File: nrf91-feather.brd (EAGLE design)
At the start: 50.8 x 22.9 mm, 126 parts, among them J2 CON-HEADER-1X12-MALE-PIN, J3 CON-HEADER-1X16-MALE-PIN, J4 CON-1909763-1, J5 CON-SIM-104224-0820, J6 CON-S2B-PH-SM4-TB(LF)(SN), J7 CON-1909763-1, J8 CON-USB-DX07S016JA1R1500, J9 CON-TC2030-MCP-NL, Q1 MOSFET-N-SC89, Q2 MOSFET-DUAL-COMP-SOT563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

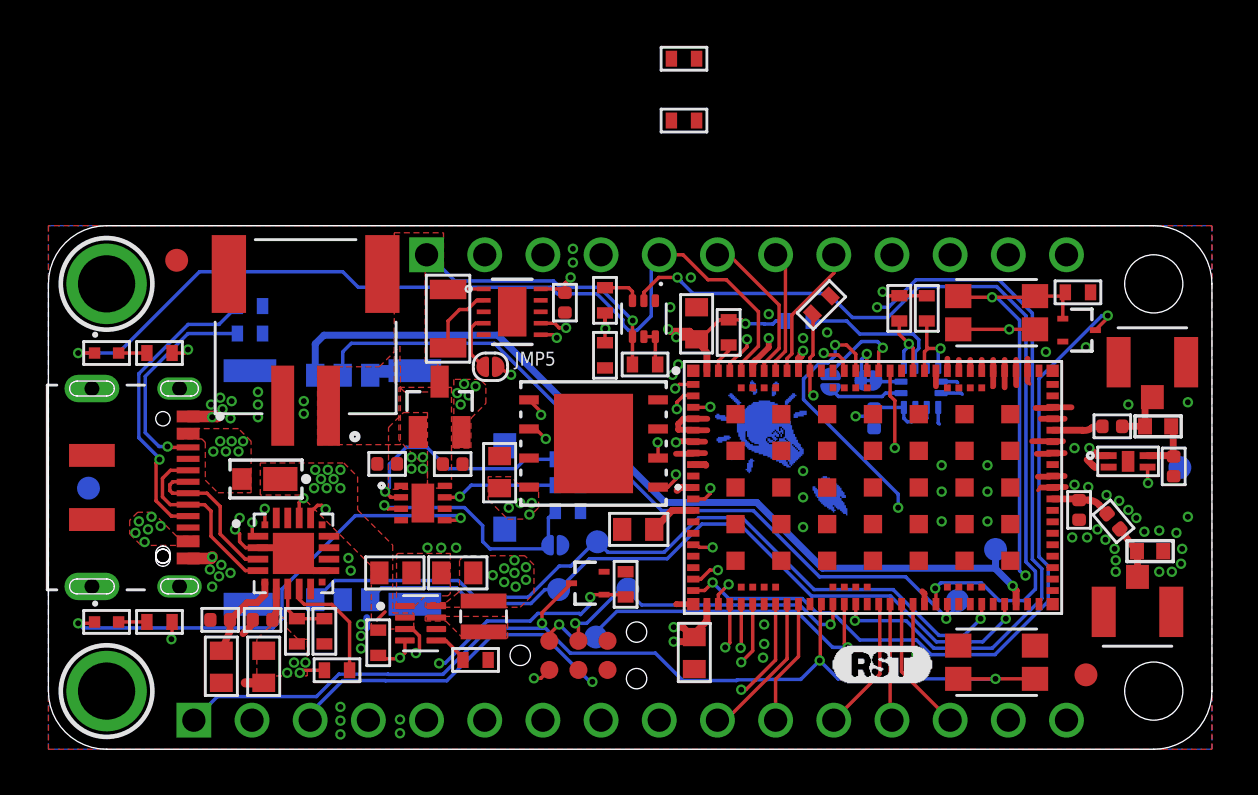
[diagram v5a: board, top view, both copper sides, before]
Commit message: Adding updated bypass and filtering for power supply
Changed:
* Ferrite and 47u for power inputs
* Re-routed battery measurement circuit
* Cleaned up
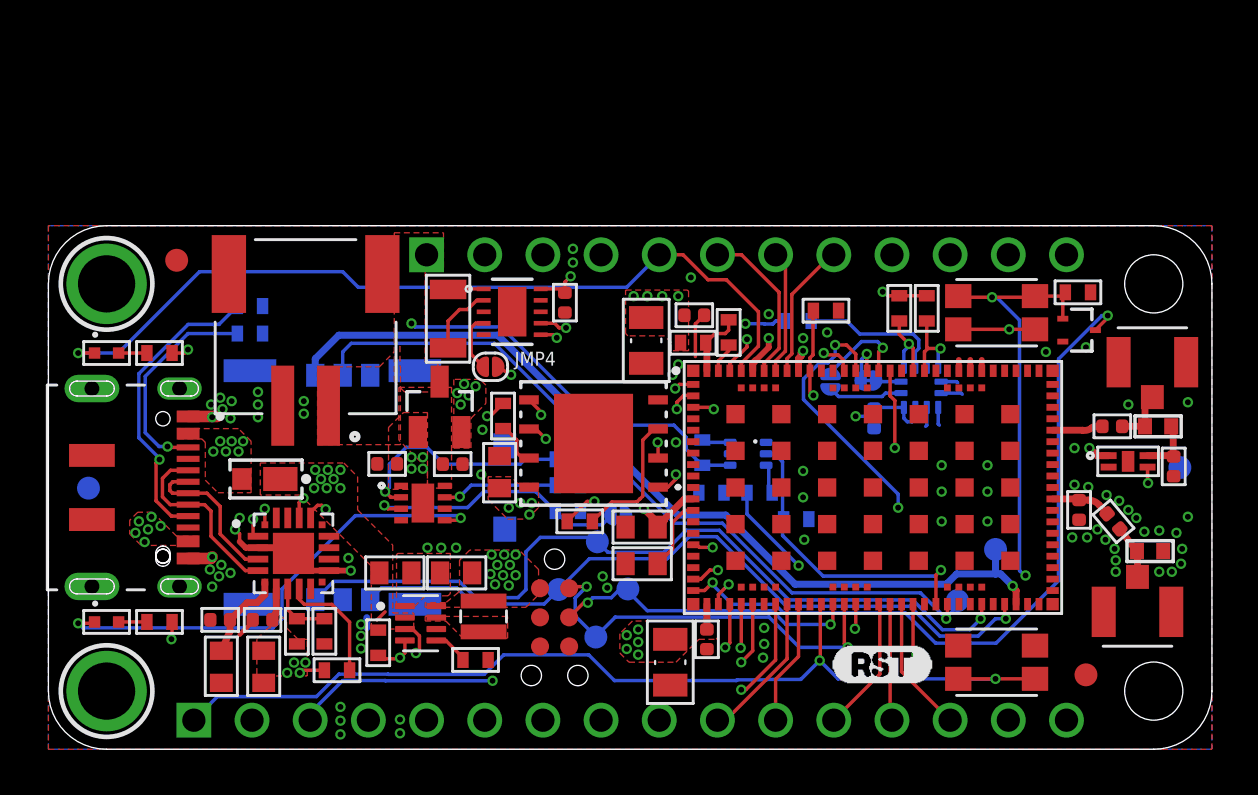
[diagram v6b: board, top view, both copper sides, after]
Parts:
- removed Q1: MOSFET-N-SC89, wolff-den:DIO_RB558WMF-L
- removed U$1: (no value), wolff-den:LOGO-CIRCUITDOJO-BULB
- added C20, C22: 0.1u, wolff-den:CAPC1005X55N
- added C21: 47u, wolff-den:C0805
- added FB1: FERRITE-120-100MHZ-0402, wolff-den:R0402-M
- C3: value 4.7u -> 47u; device wolff-den:C0603 -> wolff-den:C0805
- R9: value 100k -> 10k
- moved R23 18.1 mm to (23.2, 9.95), turned to 180 degrees
- moved R22 17.5 mm to (19.9, 14.6), turned to 90 degrees
- moved C3 14.8 mm to (27.1, 3.80), turned to 270 degrees
- moved R3 10.8 mm to (31.1, 11.2), flipped to the bottom, turned to 180 degrees
- moved R5 7.98 mm to (32.6, 10.1), flipped to the bottom, turned to 0 degrees
- moved R8 7.59 mm to (28.9, 11.2), flipped to the bottom, turned to 180 degrees
- moved Q2 7.45 mm to (30.6, 12.9), flipped to the bottom, turned to 0 degrees
- moved C8 5.96 mm to (25.9, 9.70), turned to 180 degrees
- moved R10 4.59 mm to (28.6, 12.9), flipped to the bottom, turned to 270 degrees
- moved J9 4.46 mm to (22.1, 8.30), turned to 270 degrees
- moved JMP2 3.04 mm to (24.9, 10.2)
- moved U$7 2.53 mm to (34.4, 6.30)
- moved C9 1.51 mm to (25.9, 8.10)
- moved U$6 0.78 mm to (30.3, 13.6)
- moved R1 0.32 mm to (34.0, 19.1), turned to 180 degrees
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- renumbered JMP5 to JMP4
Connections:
- removed net N$12: Q1.1, R5.2, U2.2
- new net N$16: FB1.2, R9.2, U1.102
- net !RESET: now also U2.2; no longer Q1.3
- net +3V3: now also C20.1, C21.1, C22.1, FB1.1; no longer R9.2, U1.102
- net GND: now also C20.2, C21.2, C22.2; no longer Q1.2
- net P0.25/VBAT_MEAS_EN: now also R5.2
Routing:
- net P0.20/VBAT_MEAS: track 47.3 -> 9.98 mm, vias 3 -> 2
- net P0.25/VBAT_MEAS_EN: track 37.0 -> 13.5 mm, vias 2 -> 1
- net N$12: track 22.1 -> 0.00 mm, vias 3 -> 0
- net GND: track 55.0 -> 33.1 mm, vias 84 -> 87
- net !RESET: track 46.8 -> 54.1 mm
- net N$9: track 0.00 -> 5.97 mm
- net VBAT: track 12.1 -> 16.8 mm
- net +3V3: track 21.6 -> 18.2 mm, vias 23 -> 31
- net P0.03/D7: track 39.7 -> 36.7 mm
- net N$16: track 0.00 -> 2.92 mm
- net FLASH_SCK: track 15.6 -> 12.7 mm
- net N$14: track 0.00 -> 1.99 mm
- net MODE/WAKE: track 54.9 -> 53.6 mm
- net N$5: track 2.06 -> 3.19 mm
- net CHG_TS: track 10.8 -> 11.8 mm
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
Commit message: Reconnect flash signals
Changed:
* Reconnect WP and HOLD signls
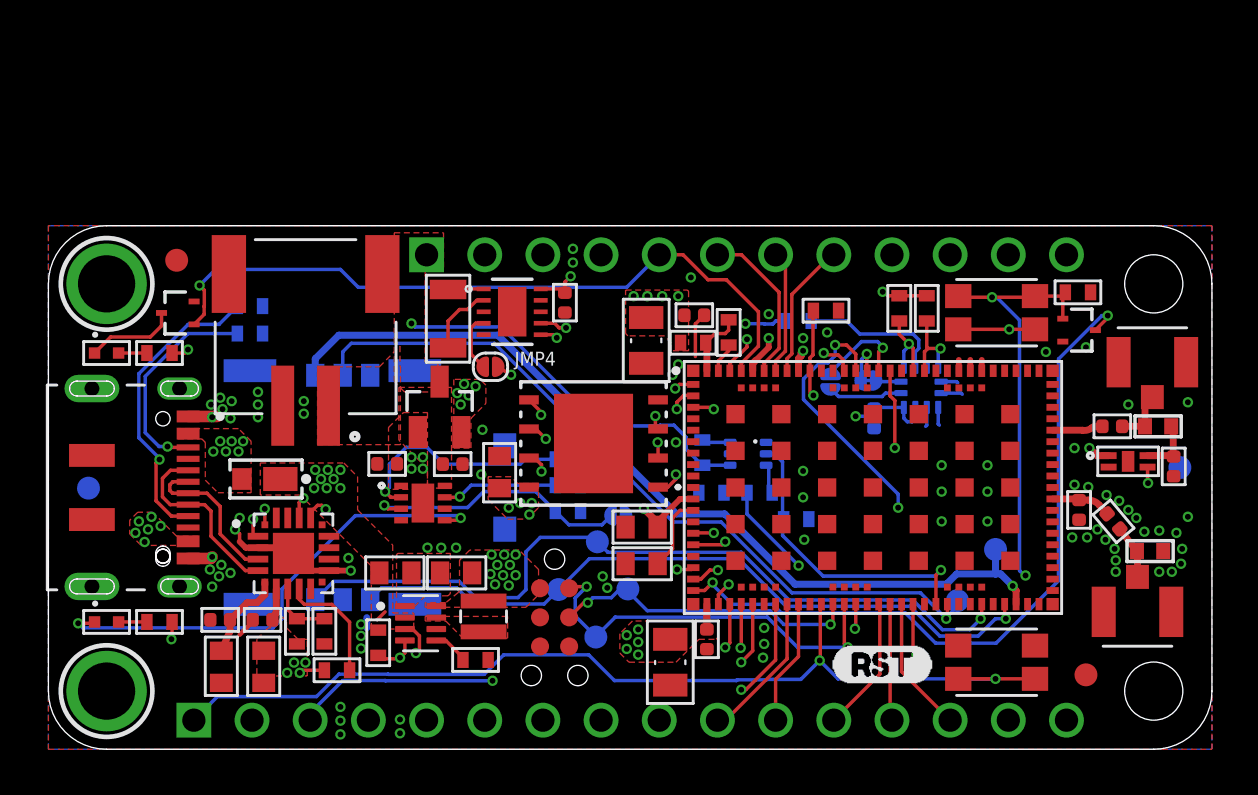
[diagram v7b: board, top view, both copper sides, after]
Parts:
- removed R22, R23: 100k, wolff-den:R0402-M
- added Q1: MOSFET-N-SC89, wolff-den:DIO_RB558WMF-L
- added R24: 100k, wolff-den:R0402-M
- R19: value 1M -> 100k
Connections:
- removed net N$14: R22.1, U6.7
- removed net N$9: R23.1, U6.3
- new net FLASH_HOLD: U1.18, U6.7
- new net FLASH_WP: U1.15, U6.3
- new net N$12: D3.C, Q1.3
- net +3V3: no longer R22.2, R23.2
- net GND: now also Q1.2, R24.1
- net P0.03/D7: now also Q1.1, R24.2; no longer D3.C
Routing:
- net FLASH_HOLD: track 0.00 -> 9.39 mm, vias 0 -> 2
- net FLASH_WP: track 0.00 -> 8.30 mm, vias 0 -> 2
- net N$9: track 5.97 -> 0.00 mm
- net P0.03/D7: track 36.7 -> 31.5 mm
- net +3V3: track 18.2 -> 13.8 mm, vias 31 -> 29
- net N$12: track 0.00 -> 3.98 mm
- net N$14: track 1.99 -> 0.00 mm
- net FLASH_SI: track 11.8 -> 12.7 mm
- net SIM_IO: track 32.3 -> 31.5 mm
- net SIM_CLK: track 35.1 -> 34.3 mm

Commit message: Consolidating parts
Changed:
* R9 to 1k
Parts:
- R9: value 10k -> 1k
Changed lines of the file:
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@@
 <attribute name="VALUE" x="5.54981875" y="6.5295" size="1.27013125" layer="28" rot="MR90"/>
 </element>
-<element name="R9" library="wolff-den" library_urn="urn:adsk.eagle:library:6370453" package="R0402-M" package3d_urn="urn:adsk.eagle:package:19061974/5" value="10k" x="29.7" y="18.2" smashed="yes" rot="R90">
-<attribute name="DESC" value="" x="17.6" y="-15.7" size="0.8128" layer="27" rot="R90" display="off"/>
-<attribute name="DIGIKEYPN" value="311-10.0KHRCT-ND" x="17.6" y="-15.7" size="0.8128" layer="27" rot="R90" display="off"/>
+<element name="R9" library="wolff-den" library_urn="urn:adsk.eagle:library:6370453" package="R0402-M" package3d_urn="urn:adsk.eagle:package:19061974/5" value="1k" x="29.7" y="18.2" smashed="yes" rot="R90">
+<attribute name="DESC" value="RES SMD 1K OHM 5% 1/16W 0402" x="17.6" y="-15.7" size="0.8128" layer="27" rot="R90" display="off"/>
+<attribute name="DIGIKEYPN" value="311-1.0KJRCT-ND" x="17.6" y="-15.7" size="0.8128" layer="27" rot="R90" display="off"/>
 <attribute name="MF" value="" x="17.6" y="-15.7" size="0.8128" layer="27" rot="R90" display="off"/>
-<attribute name="MPN" value="RC0603FR-0710KL" x="17.6" y="-15.7" size="0.8128" layer="27" rot="R90" display="off"/>
+<attribute name="MPN" value="RC0402JR-071KL" x="17.6" y="-15.7" size="0.8128" layer="27" rot="R90" display="off"/>
 <attribute name="NAME" x="29.7" y="18.2" size="0.2" layer="51" rot="R90" align="center"/>
-<attribute name="POWER" value="" x="17.6" y="-15.7" size="0.8128" layer="27" rot="R90" display="off"/>
-<attribute name="TEMPHIGH" value="155" x="29.7" y="18.2" size="1.778" layer="27" rot="R90" display="off"/>
-<attribute name="TEMPLOW" value="-55" x="29.7" y="18.2" size="1.778" layer="27" rot="R90" display="off"/>
-<attribute name="TOLERANCE" value="1%" x="17.6" y="-15.7" size="0.8128" layer="27" rot="R90" display="off"/>
+<attribute name="POWER" value="1/16W" x="17.6" y="-15.7" size="0.8128" layer="27" rot="R90" display="off"/>
+<attribute name="TEMPHIGH" value="" x="29.7" y="18.2" size="1.778" layer="27" rot="R90" display="off"/>
+<attribute name="TEMPLOW" value="" x="29.7" y="18.2" size="1.778" layer="27" rot="R90" display="off"/>
+<attribute name="TOLERANCE" value="5%" x="17.6" y="-15.7" size="0.8128" layer="27" rot="R90" display="off"/>
 </element>
 <element name="C8" library="wolff-den" library_urn="urn:adsk.eagle:library:6370453" package="C0603" package3d_urn="urn:adsk.eagle:package:5807321/8" value="4.7u" x="25.9" y="9.7" smashed="yes" rot="R180">
